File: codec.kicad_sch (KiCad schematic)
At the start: 1 part, among them U1 UDA1380HN_N2

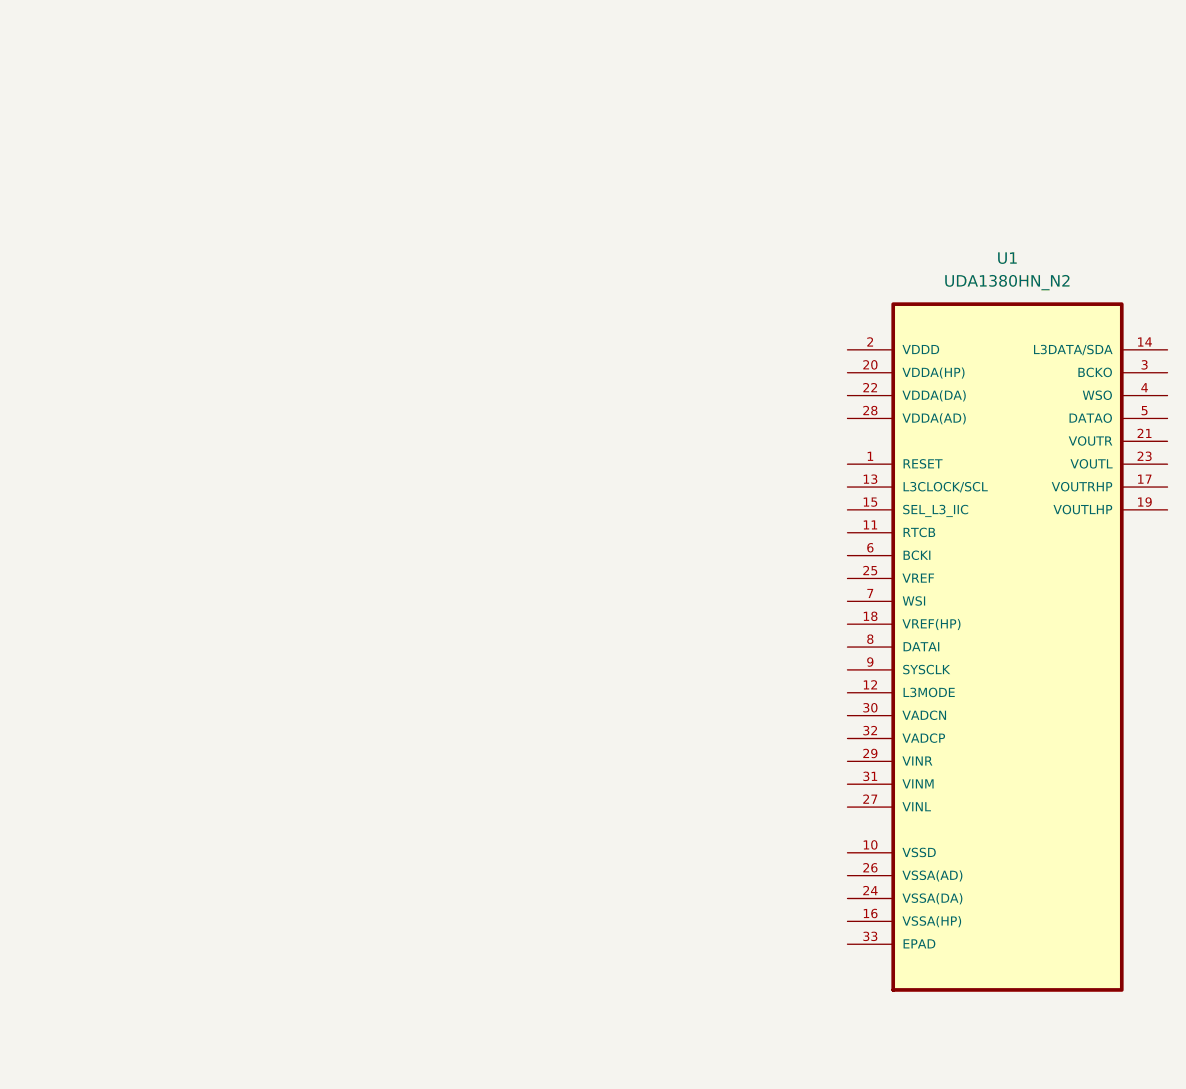
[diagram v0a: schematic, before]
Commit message: Components for audio codec part 1
reading from data sheet application, page 61
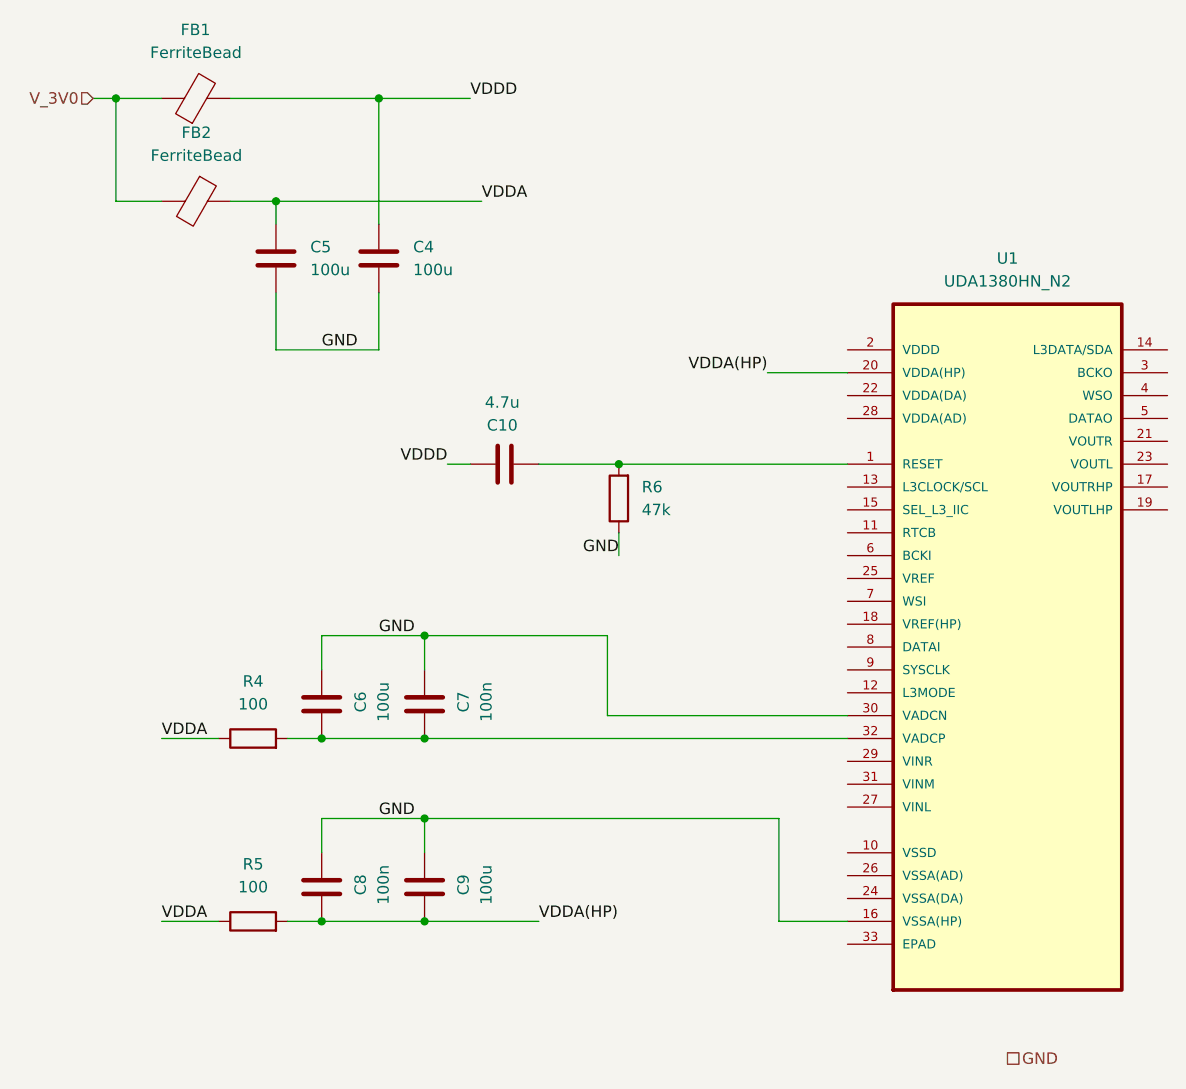
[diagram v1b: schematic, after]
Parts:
- added C10: 4.7u, symbol Device:C
- added C4, C5, C6, C9: 100u, symbol Device:C
- added C7, C8: 100n, symbol Device:C
- added FB1, FB2: FerriteBead, symbol Device:FerriteBead
- added R4, R5: 100, symbol Device:R
- added R6: 47k, symbol Device:R
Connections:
- net at U1.1 (RESET): now also C10.2, R6.2
- net GND: now reaches U1.16 (VSSA(HP))
- net GND: now also U1.30 (VADCN), C4.2, C5.2, C6.1, C7.1, C8.1, C9.1, R6.1
- net VDDA(HP): now reaches U1.20 (VDDA(HP))
- net VDDA(HP): now also C8.2, C9.2, R5.2
- net at U1.32 (VADCP): now also C6.2, C7.2, R4.2
- new net VDDA: C5.1, FB2.1, R4.1, R5.1
- new net VDDD: C10.1, C4.1, FB1.2
- new net V_3V0: FB1.1, FB2.2

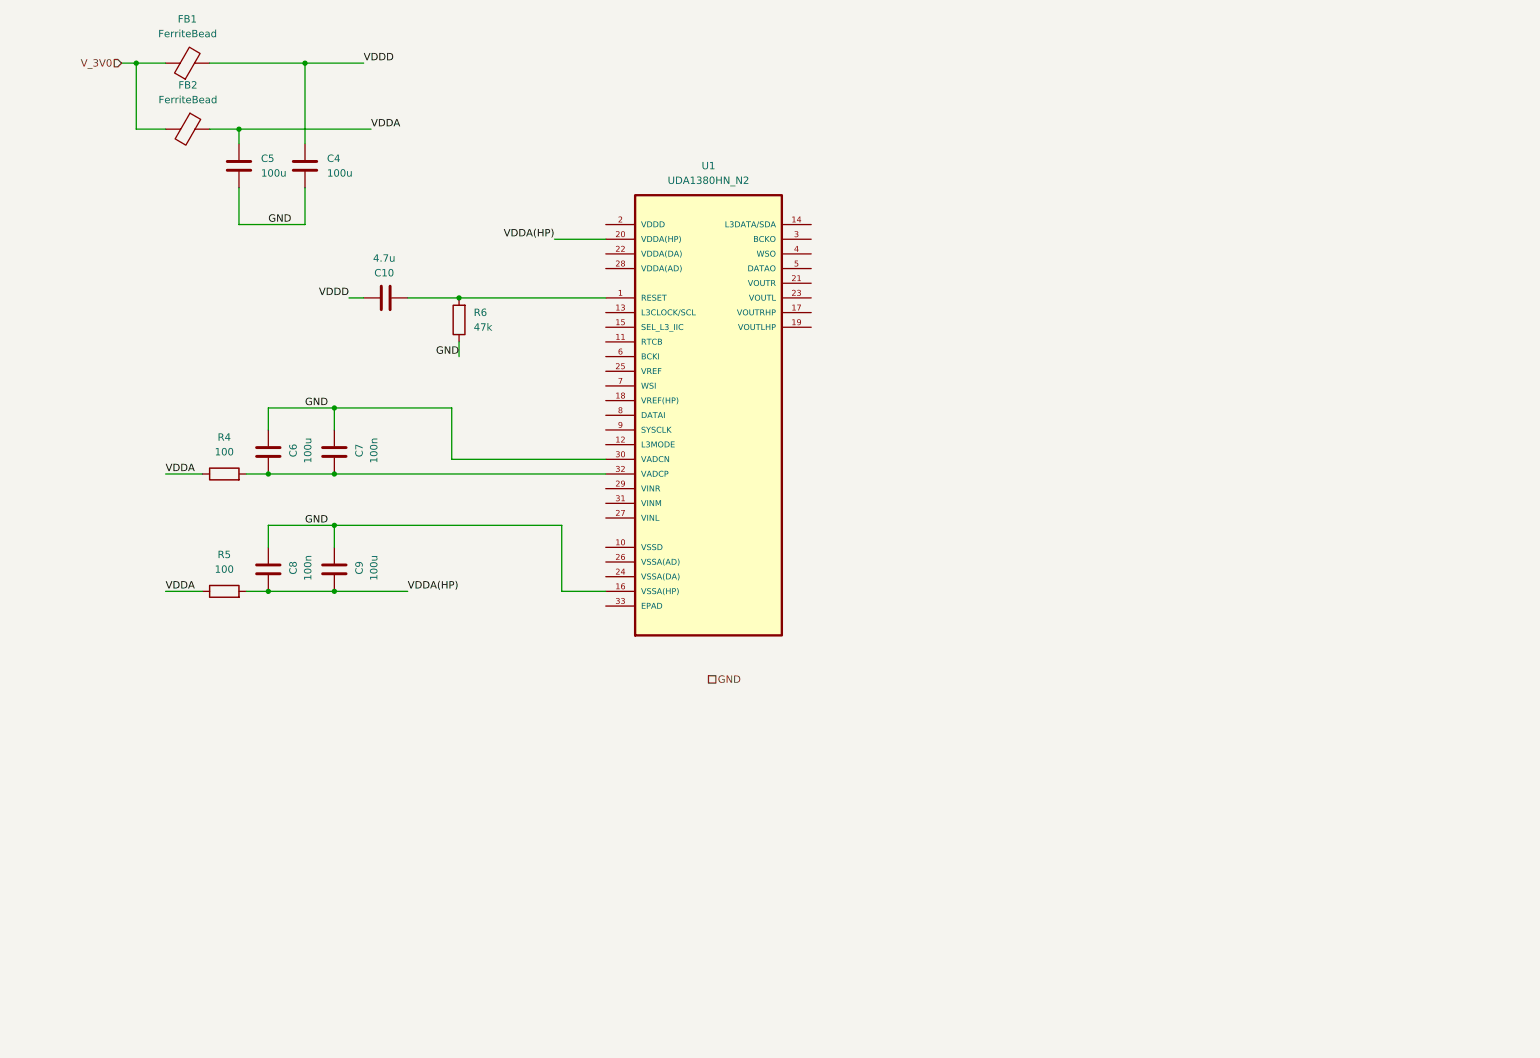
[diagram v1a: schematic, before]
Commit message: Added more parts to codec
VDD and VDDA related pins, and organized a bit
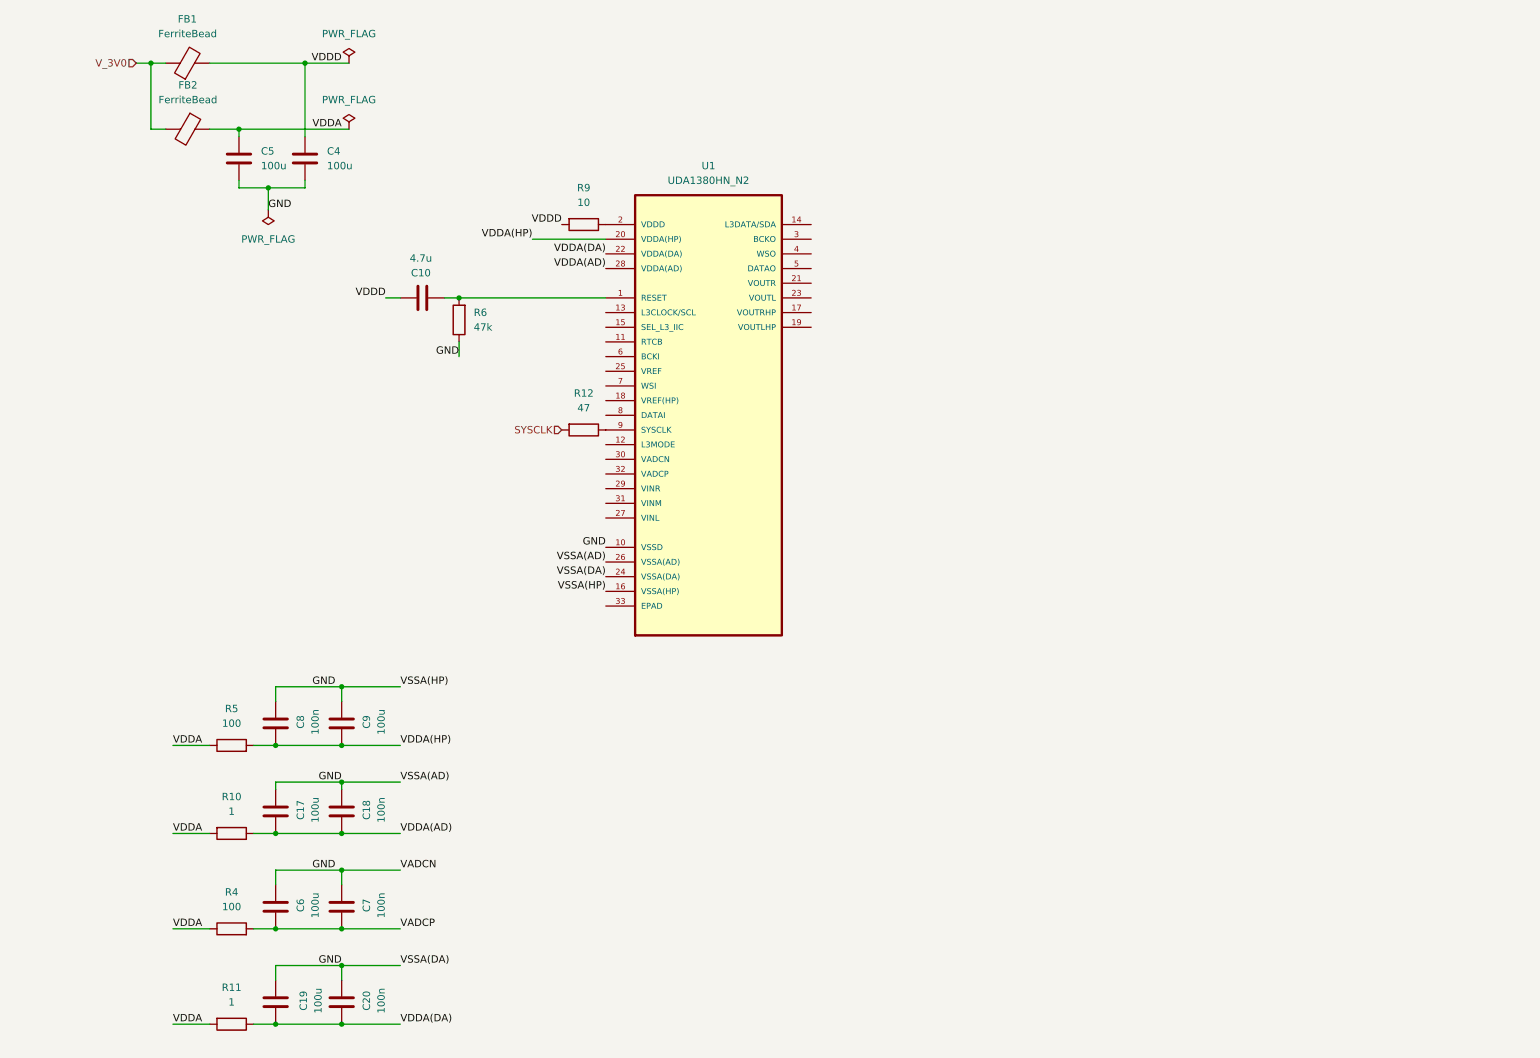
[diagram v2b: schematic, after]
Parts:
- added C17, C19: 100u, symbol Device:C
- added C18, C20: 100n, symbol Device:C
- added R10, R11: 1, symbol Device:R
- added R12: 47, symbol Device:R
- added R9: 10, symbol Device:R
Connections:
- net GND: now also U1.10 (VSSD), U1.24 (VSSA(DA)), U1.26 (VSSA(AD)), C17.1, C18.1, C19.1, C20.1; no longer U1.30 (VADCN)
- net VDDA: now also R10.2, R11.2
- net VDDD: now also R9.2
- net VADCP: now reaches C6.2, C7.2, R4.2
- net VADCP: no longer U1.32 (VADCP)
- net at U1.2 (VDDD): now also R9.1
- net VDDA(DA): now reaches U1.22 (VDDA(DA))
- net VDDA(DA): now also C19.2, C20.2, R11.1
- net VDDA(AD): now reaches U1.28 (VDDA(AD))
- net VDDA(AD): now also C17.2, C18.2, R10.1
- net at U1.9 (SYSCLK): now also R12.1
- new net SYSCLK: R12.2
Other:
- moved on the sheet: C10, C4, C5, C6, C7, C8, C9, R4, R5

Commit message: Organized codec and imported pins
Also changed color of microchips in main
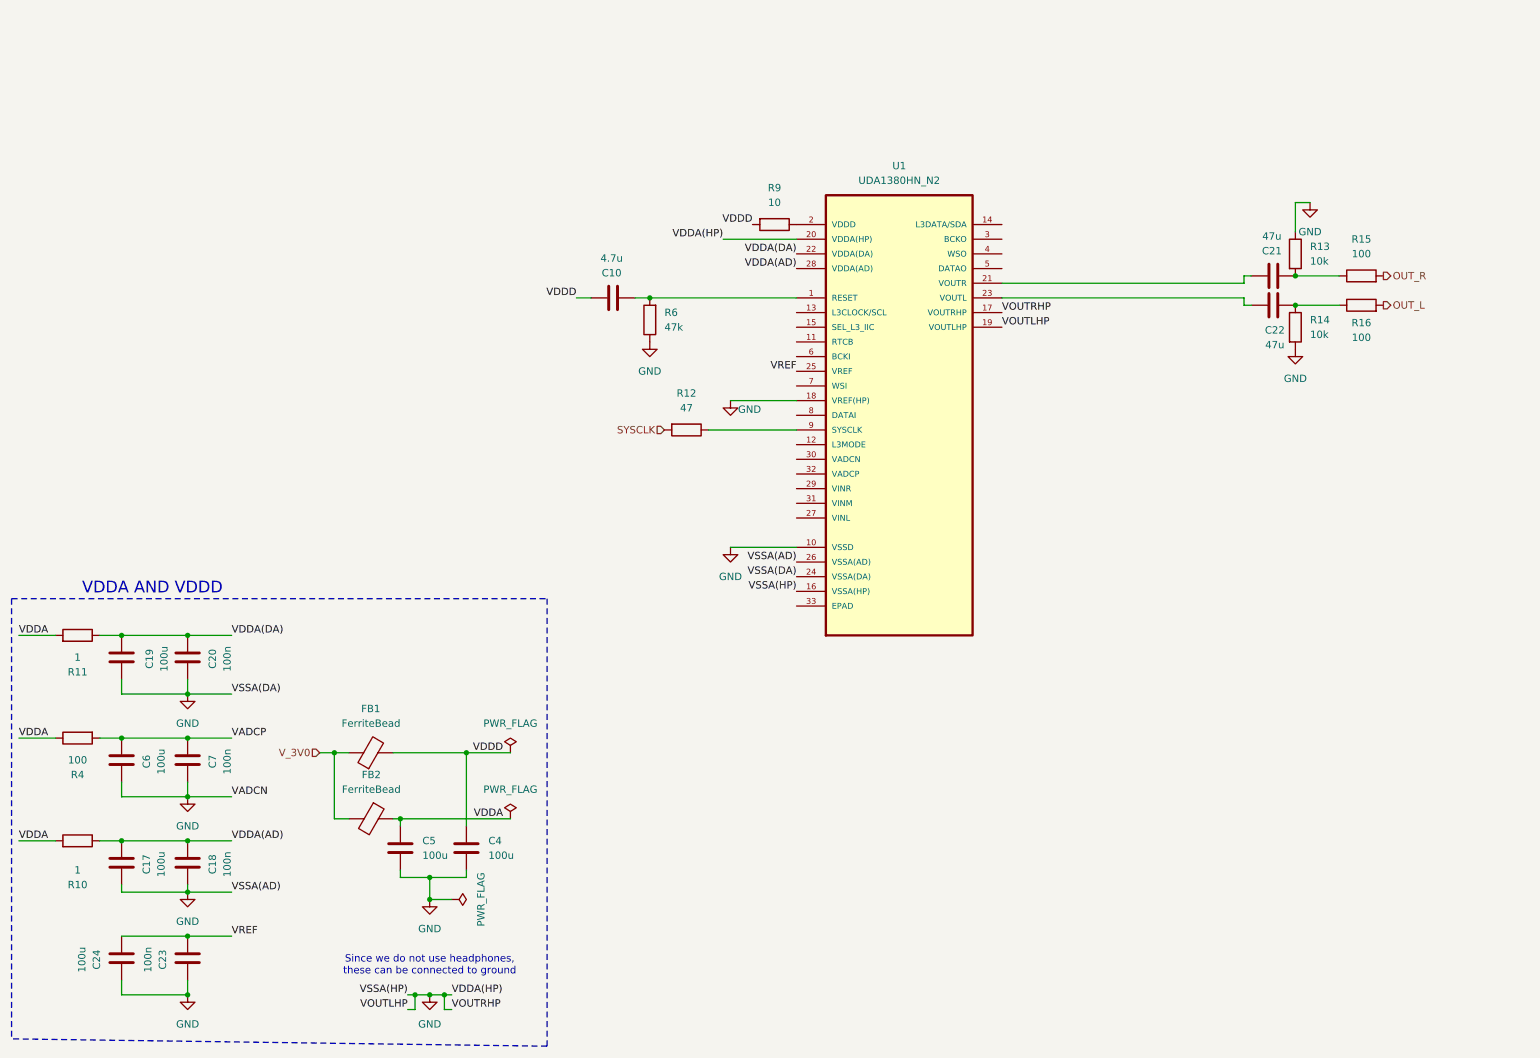
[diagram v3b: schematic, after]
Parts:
- removed C8: 100n, symbol Device:C
- removed C9: 100u, symbol Device:C
- removed R5: 100, symbol Device:R
- added C21, C22: 47u, symbol Device:C
- added C23: 100n, symbol Device:C
- added C24: 100u, symbol Device:C
- added R13, R14: 10k, symbol Device:R
- added R15, R16: 100, symbol Device:R
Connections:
- net VDDA(HP) is gone; now on net GND: U1.20 (VDDA(HP))
- net GND: now also U1.17 (VOUTRHP), U1.18 (VREF(HP)), U1.19 (VOUTLHP), C23.1, C24.1, R13.1, R14.2
- net at U1.21 (VOUTR): now also C21.1
- net at U1.23 (VOUTL): now also C22.2
- net VREF: now reaches U1.25 (VREF)
- net VREF: now also C23.2, C24.2
- new net: C21.2, R13.2, R15.1
- new net: C22.1, R14.1, R16.1
- new net OUT_L: R16.2
- new net OUT_R: R15.2
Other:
- note added: "Since we do not use headphones, these can be connected to ground"
- note added: "VDDA AND VDDD"
- moved on the sheet: C10, C17, C18, C19, C20, C4, C5, C6, C7, FB1, FB2, R10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

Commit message: Added notes to codec
About EPAD, microphone and speaker
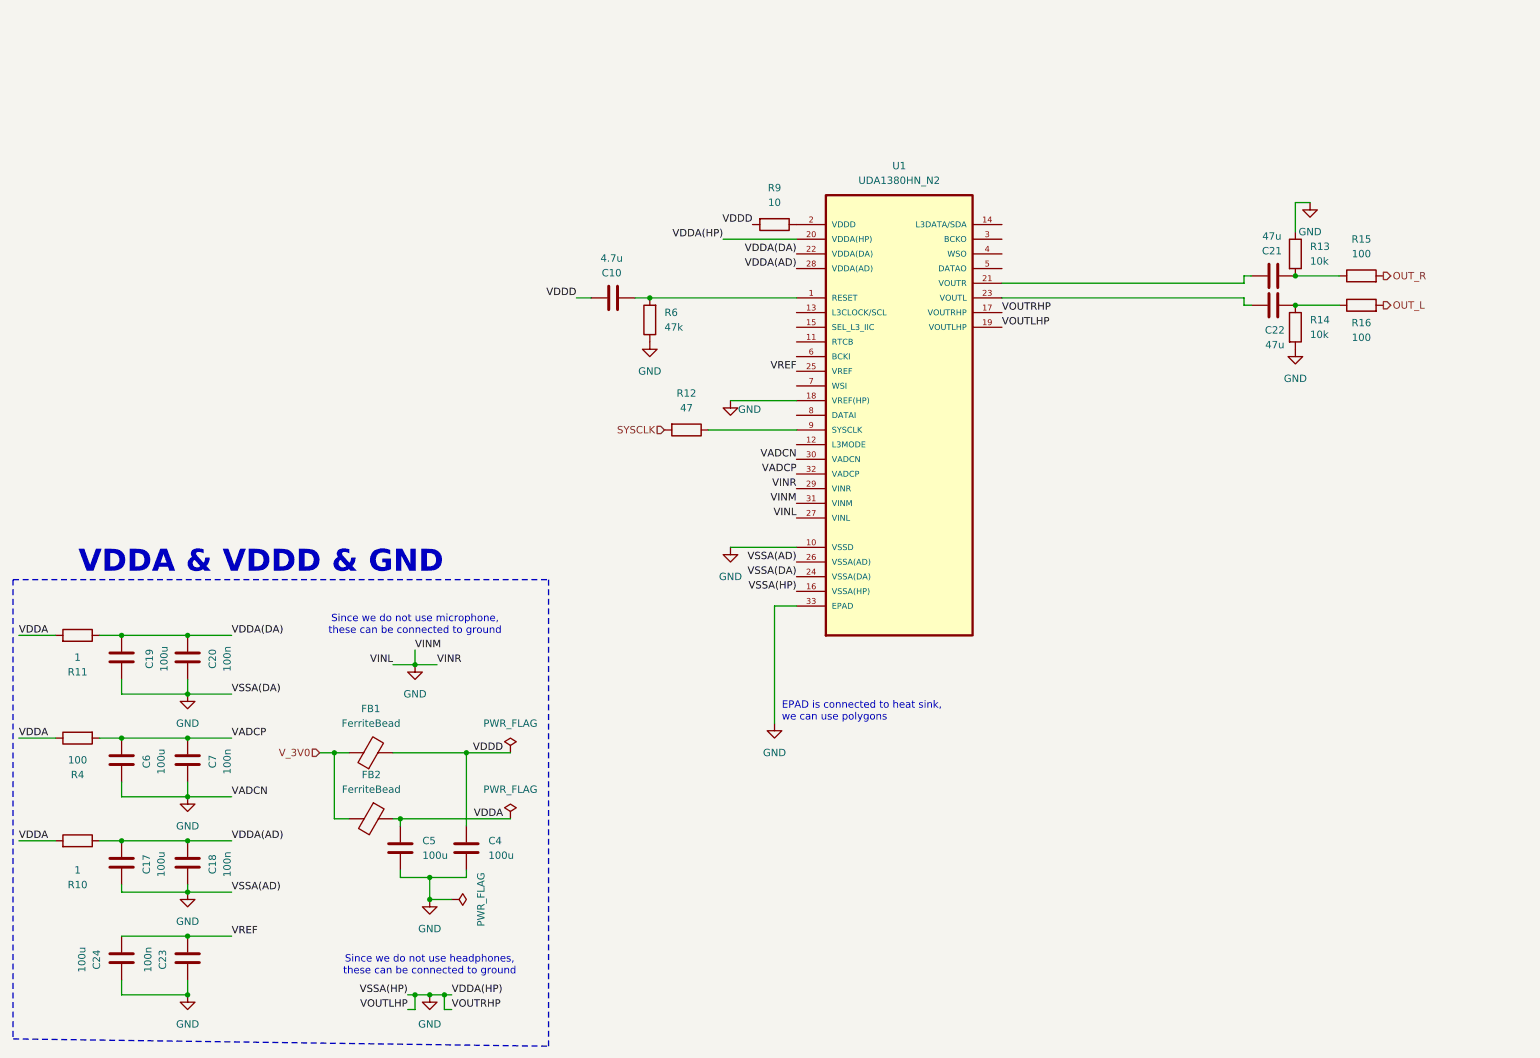
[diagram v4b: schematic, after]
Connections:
- net GND: now also U1.27 (VINL), U1.29 (VINR), U1.30 (VADCN), U1.31 (VINM), U1.33 (EPAD)
- net VADCP: now also U1.32 (VADCP)
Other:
- note added: "EPAD is connected to heat sink, we can use polygons"
- note added: "Since we do not use microphone, these can be connected to ground"
- note added: "VDDA & VDDD & GND"
- note removed: "VDDA AND VDDD"
